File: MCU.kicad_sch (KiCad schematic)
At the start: 30 parts, among them J7 Conn_01x04, J8 PinHeader_2x5_P1.27mm_SMD, SW1 SW_KSC441J70SHLFS_SMD, SW2 SW_KSC441J70SHLFS_SMD, U3 STM32U585CIT3, Y1 Oscillator_40MHz_YIC_OSC-S5

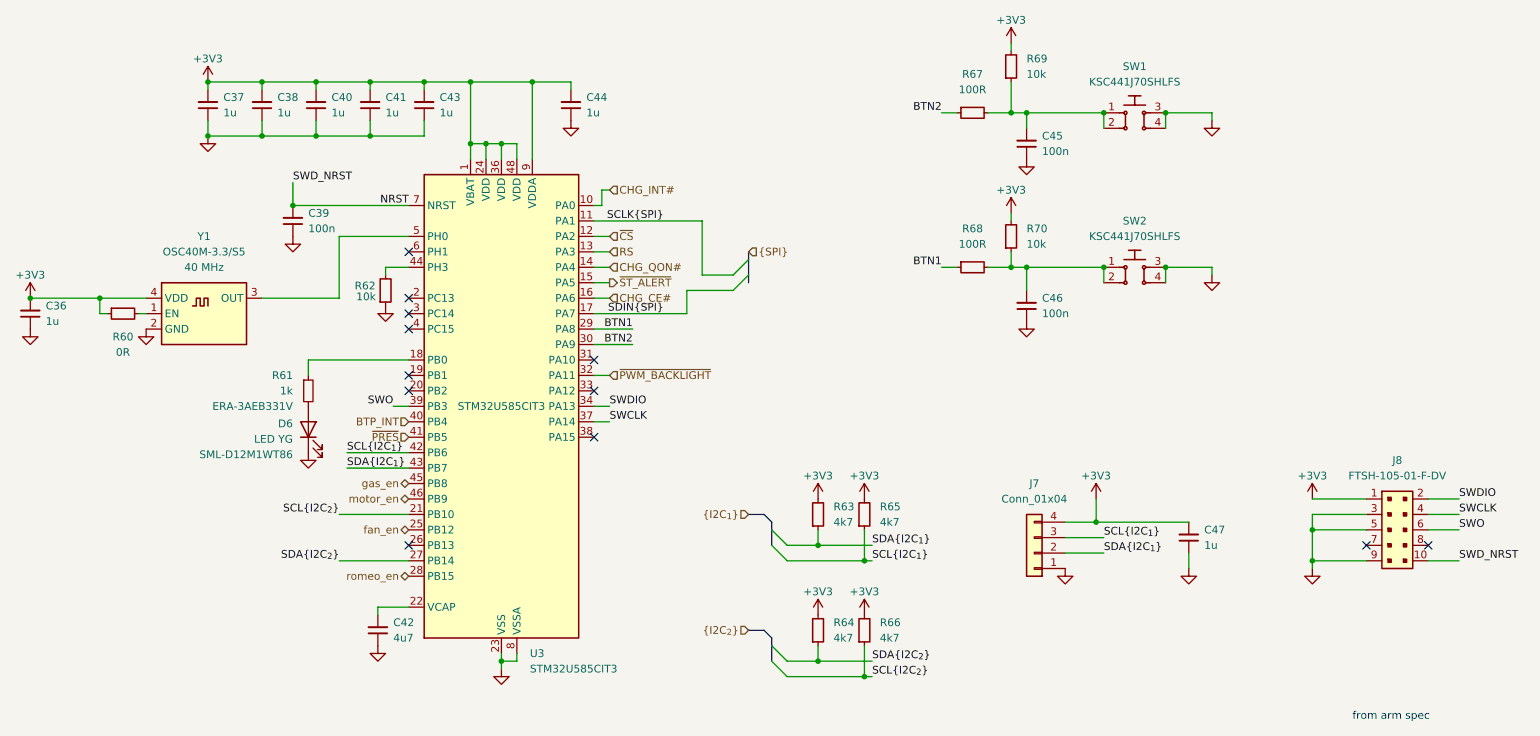
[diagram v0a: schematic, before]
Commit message: Minimal version without BMS
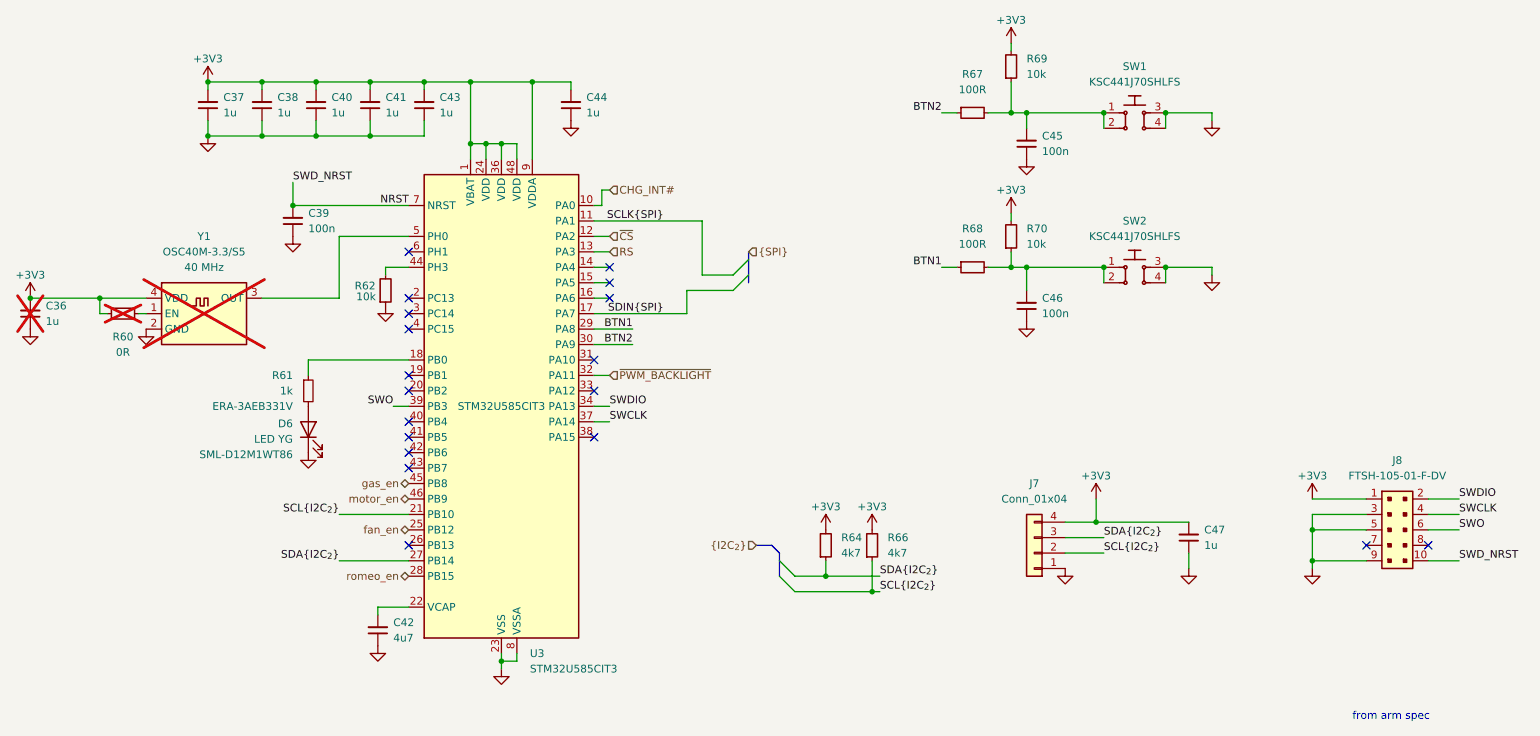
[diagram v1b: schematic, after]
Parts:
- removed R63, R65: R_4k7_0402, Hardware Components Footprints:R_0402_1005Metric, symbol lib:R_4k7_0402
- C36, R60, Y1: now not fitted
- J7: footprint (none) -> Hardware Components Footprints:Conn_JST_XH_1x4_B4B-XH-A-LF-SN
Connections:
- net SCL{I2C_{2}}: now also J7.2 (Pin_2)
- net SDA{I2C_{2}}: now also J7.3 (Pin_3)
- net BTP_INT: no longer names the net of U3.40 (PB4)
- net CHG_CE#: no longer names the net of U3.16 (PA6)
- net CHG_QON#: no longer names the net of U3.14 (PA4)
- net SCL{I2C_{1}}: no longer names the net of U3.42 (PB6)
- net SCL{I2C_{1}}: no longer J7.3 (Pin_3)
- net SDA{I2C_{1}}: no longer names the net of U3.43 (PB7)
- net SDA{I2C_{1}}: no longer J7.2 (Pin_2)
- net ~{PRES}: no longer names the net of U3.41 (PB5)
- net ~{ST_ALERT}: no longer names the net of U3.15 (PA5)
- no-connect marks 12 -> 19
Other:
- moved on the sheet: R64, R66
